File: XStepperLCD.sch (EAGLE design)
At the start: 7 parts, among them U1 Attiny85

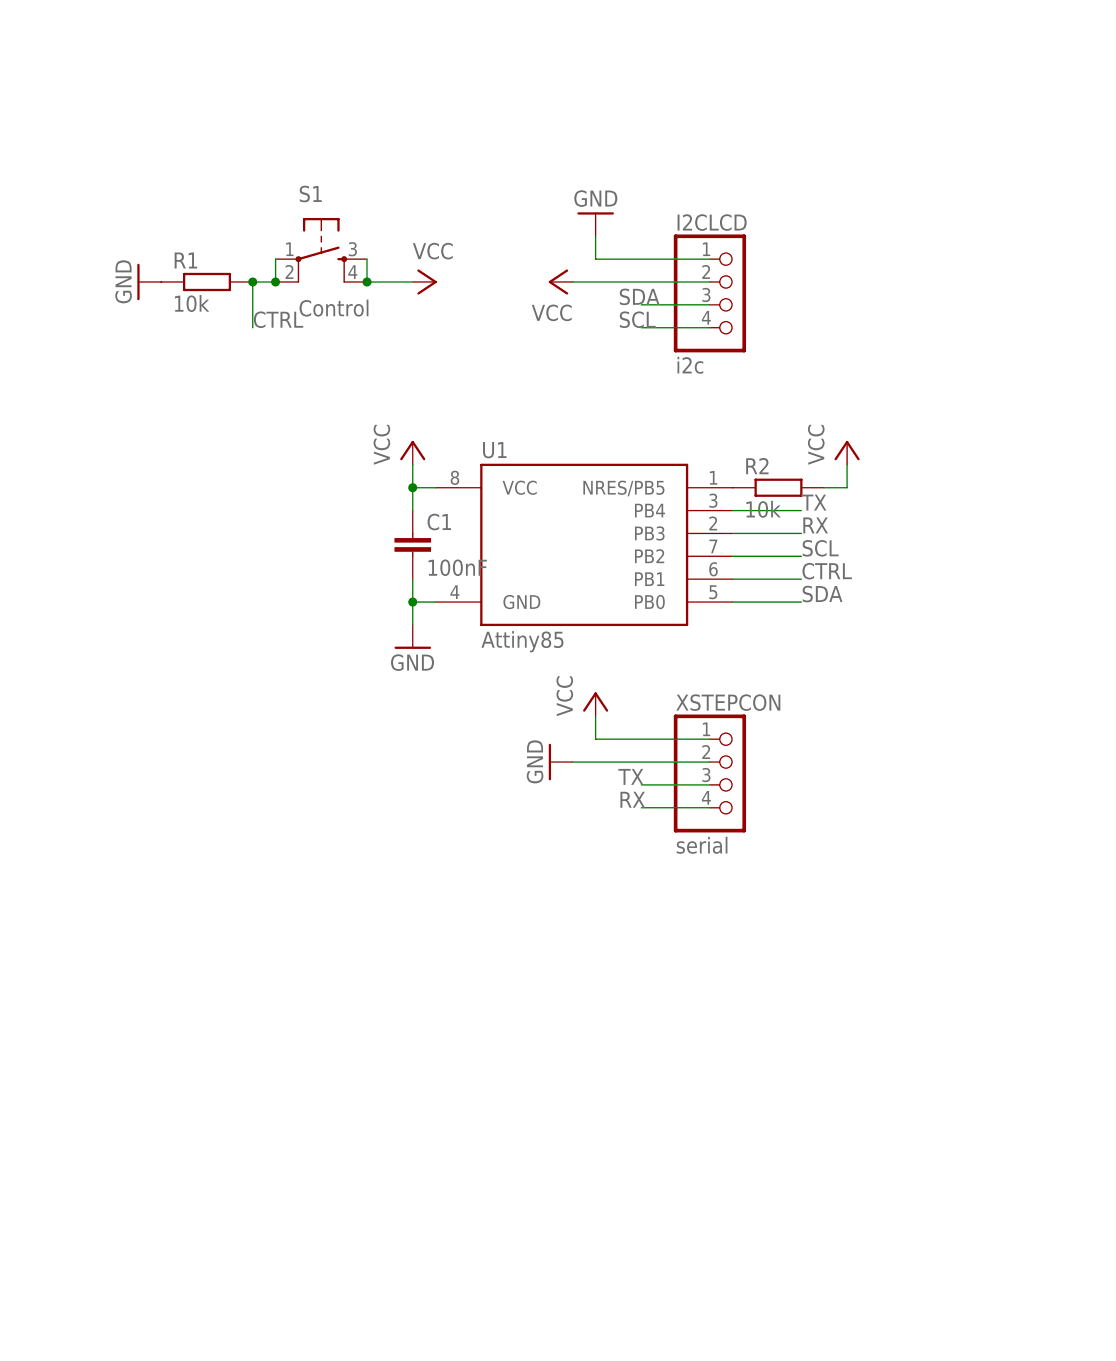
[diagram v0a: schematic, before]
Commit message: First konzept for XLCD with 328p
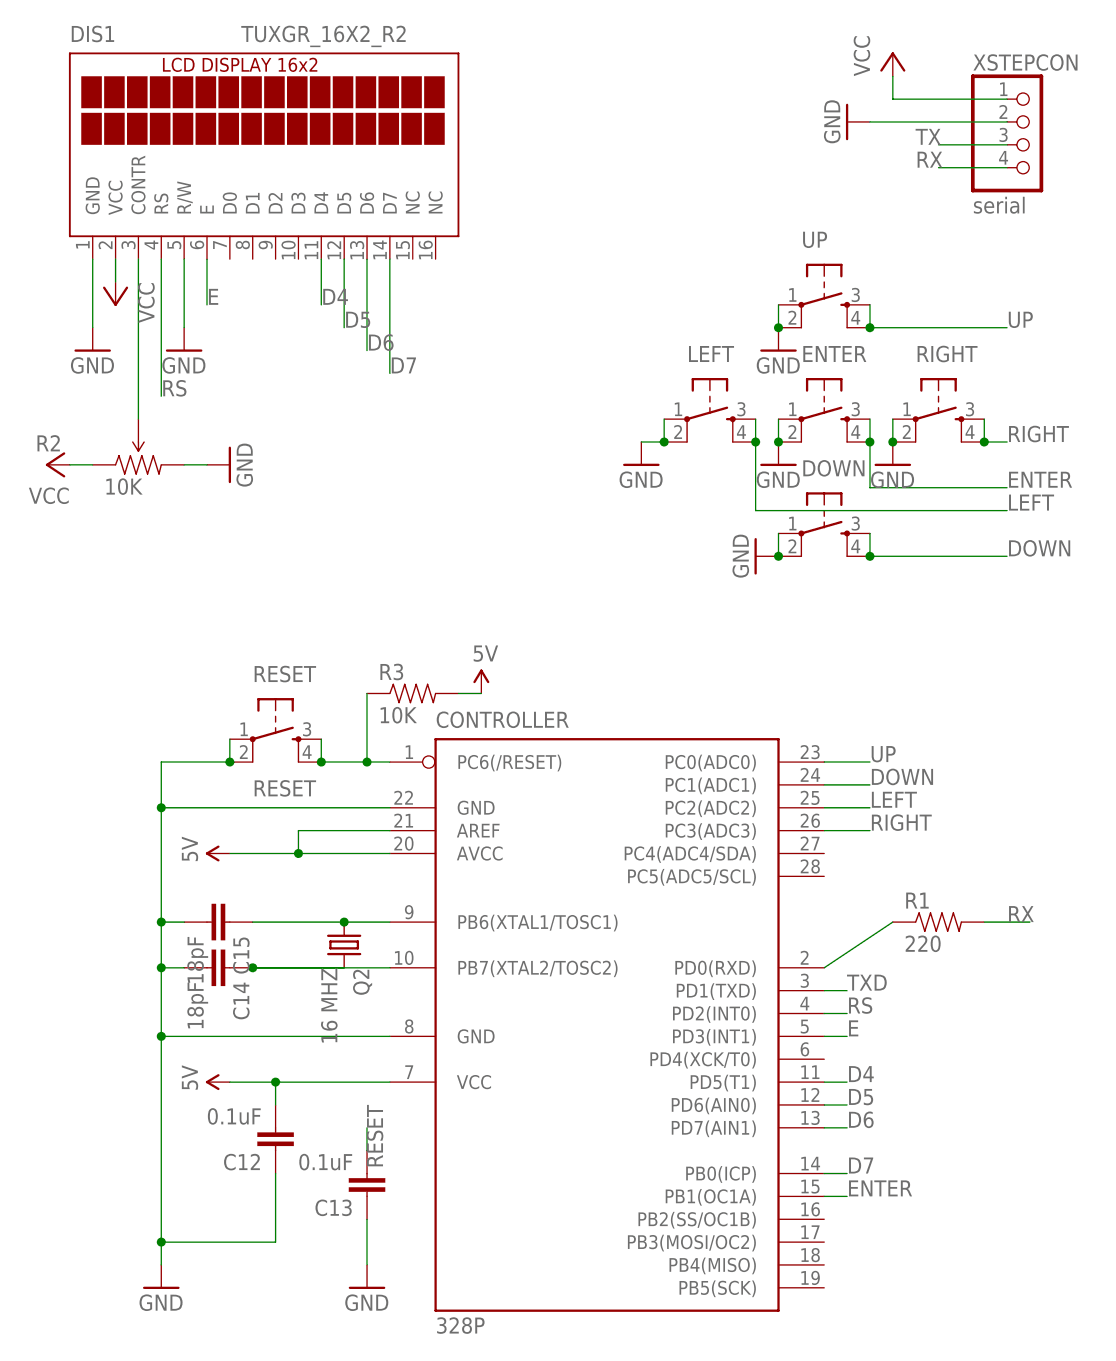
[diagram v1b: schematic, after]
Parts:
- removed C1: 100nF, rcl:C-EU025-025X050
- removed I2CLCD: i2c, pinhead:PINHD-1X4/90
- removed S1: Control, SparkFun-Electromechanical:TAC_SWITCHPTH
- removed U1: Attiny85, _hhn_attiny25_45_85:ATTINY85V-10P
- added 328P: CONTROLLER, Bibsatmel:MEGA8-P
- added C12, C13: 0.1uF, resistor:C-EU025-025X050
- added C14, C15: 18pF, resistor:C-EU025-025X050
- added DIS1: TUXGR_16X2_R2, display-lcd:TUXGR_16X2_R2
- added DOWN, ENTER, LEFT, RIGHT, UP: (no value), SparkFun:TAC_SWITCHPTH
- added Q2: 16 MHZ, crystal:CRYSTALHC49S
- added R3: 10K, SparkFun-Resistors:RESISTORAXIAL-0.3
- added RESET: RESET, SparkFun:TAC_SWITCHPTH
- R1: value 10k -> 220; device resistor:R-EU_0204/7 -> SparkFun-Resistors:RESISTORAXIAL-0.3
- R2: value 10k -> 10K; device resistor:R-EU_0204/7 -> SparkFun-Electromechanical:TRIMPOT-PTH-KNOB
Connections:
- removed net CTRL: R1.2, S1.1, S1.2, U1.PB1
- removed net SCL: I2CLCD.4, U1.PB2
- removed net SDA: I2CLCD.3, U1.PB0
- new net 5V: 328P.AREF, 328P.AVCC, 328P.VCC@1, C12.2, R3.2
- new net D4: 328P.PD5(T1), DIS1.D4
- new net D5: 328P.PD6(AIN0), DIS1.D5
- new net D6: 328P.PD7(AIN1), DIS1.D6
- new net D7: 328P.PB0(ICP), DIS1.D7
- new net DOWN: 328P.PC1(ADC1), DOWN.3, DOWN.4
- new net E: 328P.PD3(INT1), DIS1.E
- new net ENTER: 328P.PB1(OC1A), ENTER.3, ENTER.4
- new net LEFT: 328P.PC2(ADC2), LEFT.3, LEFT.4
- new net N$2: DIS1.CONTR, R2.WIPER
- new net N$33: 328P.PB6(XTAL1/TOSC1), C15.1, Q2.1
- new net N$34: 328P.PB7(XTAL2/TOSC2), C14.1, Q2.2
- new net RESET: 328P.PC6(/RESET), C13.2, R3.1, RESET.3, RESET.4
- new net RIGHT: 328P.PC3(ADC3), RIGHT.3, RIGHT.4
- new net RS: 328P.PD2(INT0), DIS1.RS
- new net TXD: 328P.PD1(TXD)
- new net UP: 328P.PC0(ADC0), UP.3, UP.4
- net GND: now also 328P.GND, 328P.GND@1, C12.1, C13.1, C14.2, C15.2, DIS1.GND, DIS1.R/W, DOWN.1, DOWN.2, ENTER.1, ENTER.2, LEFT.1, LEFT.2, R2.CW, RESET.1, RESET.2, RIGHT.1, RIGHT.2, UP.1, UP.2; no longer C1.2, I2CLCD.1, R1.1, U1.GND
- net N$1: now also 328P.PD0(RXD), R1.1; no longer R2.1, U1.NRES/PB5
- net RX: now also R1.2; no longer U1.PB3
- net TX: no longer U1.PB4
- net VCC: now also DIS1.VCC, R2.CCW; no longer C1.1, I2CLCD.2, R2.2, S1.3, S1.4, U1.VCC
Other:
- moved on the sheet: XSTEPCON

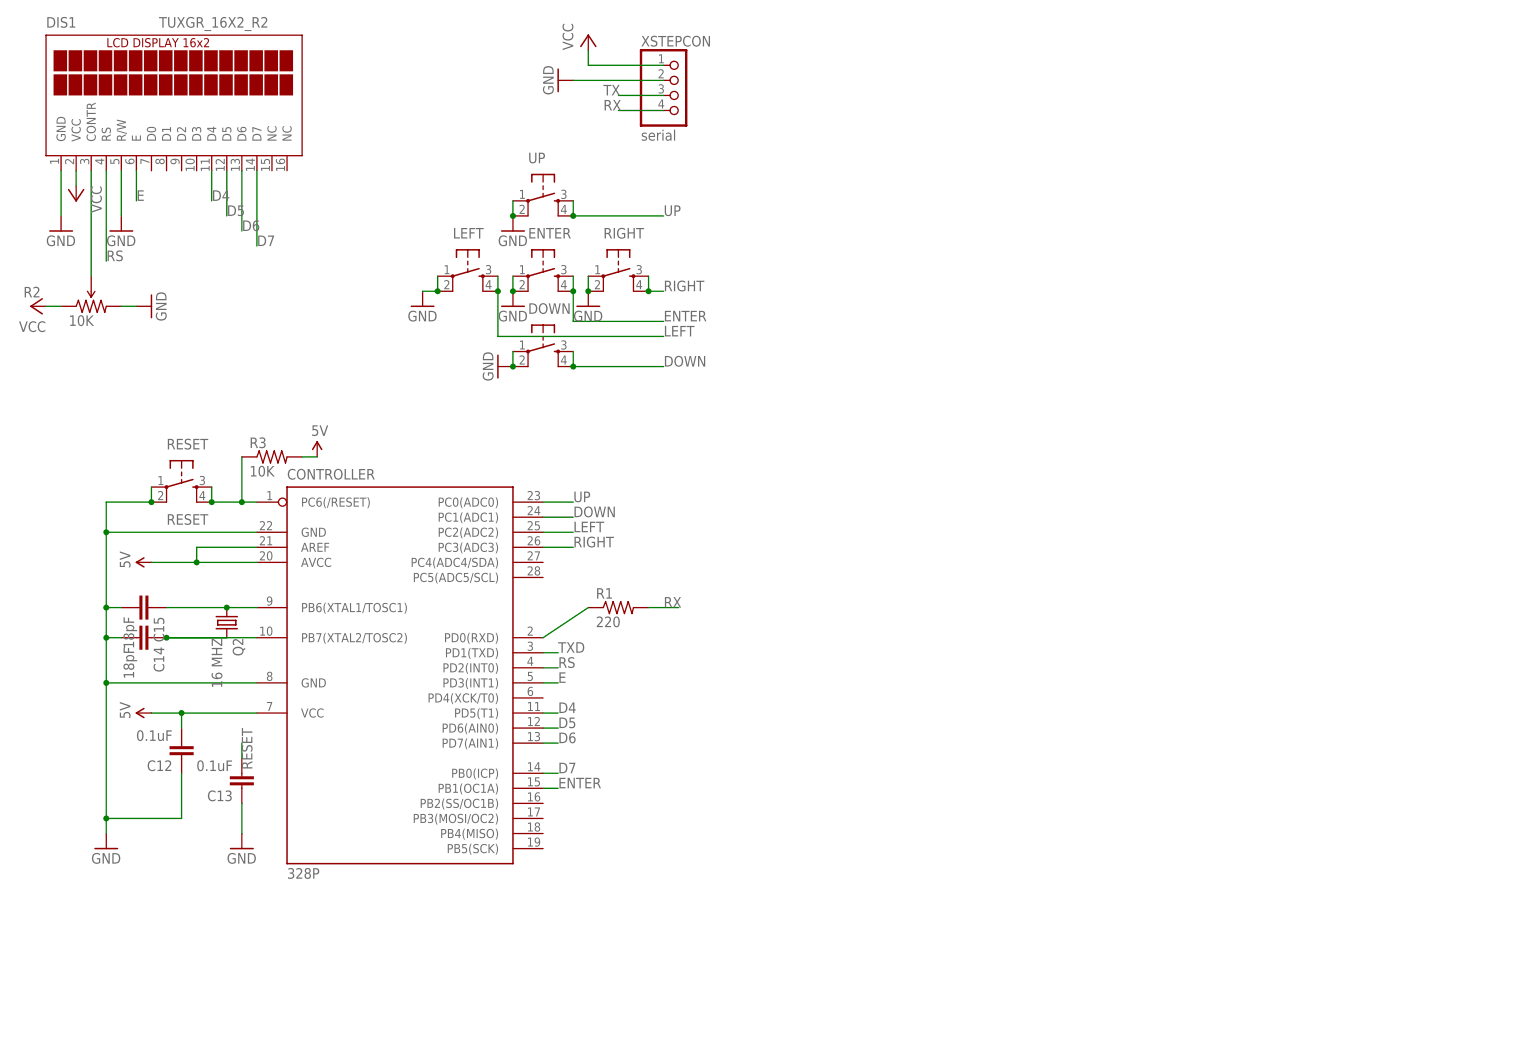
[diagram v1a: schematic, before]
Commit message: add conn header for buttons
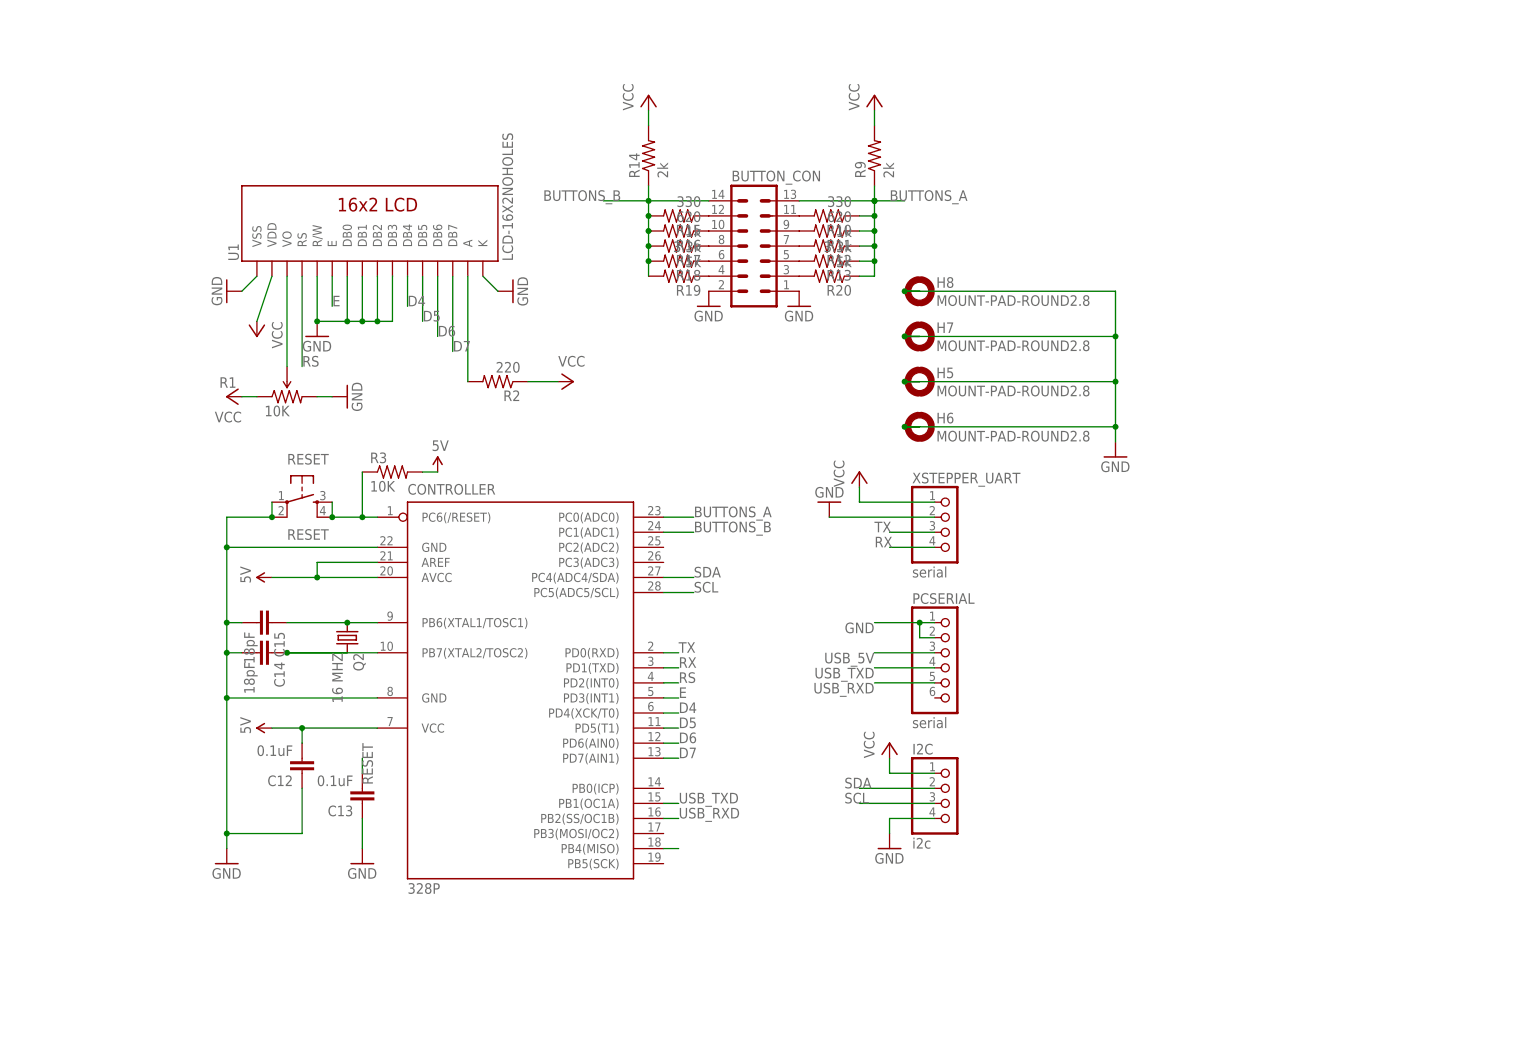
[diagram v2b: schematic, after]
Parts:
- removed DIS1: TUXGR_16X2_R2, display-lcd:TUXGR_16X2_R2
- removed DOWN, ENTER, LEFT, RIGHT, UP: (no value), SparkFun:TAC_SWITCHPTH
- removed XSTEPCON: serial, pinhead:PINHD-1X4/90
- added BUTTON_CON: (no value), con-ml:ML14
- added H5, H6, H7, H8: MOUNT-PAD-ROUND2.8, holes:MOUNT-PAD-ROUND2.8
- added I2C: i2c, pinhead:PINHD-1X4/90
- added PCSERIAL: serial, pinhead:PINHD-1X6/90
- added R10, R15: 330, SparkFun-Resistors:RESISTORAXIAL-0.3
- added R11, R16: 620, SparkFun-Resistors:RESISTORAXIAL-0.3
- added R12, R17: 1k, SparkFun-Resistors:RESISTORAXIAL-0.3
- added R13, R18: 3.3k, SparkFun-Resistors:RESISTORAXIAL-0.3
- added R14, R9: 2k, SparkFun-Resistors:RESISTORAXIAL-0.3
- added R19, R20: 5k, SparkFun-Resistors:RESISTORAXIAL-0.3
- added U1: LCD-16X2NOHOLES, SparkFun-Displays:LCD-16X2NOHOLES
- added XSTEPPER_UART: serial, pinhead:PINHD-1X4/90
- R1: value 220 -> 10K; device SparkFun-Resistors:RESISTORAXIAL-0.3 -> SparkFun-Electromechanical:TRIMPOT-PTH-KNOB
- R2: value 10K -> 220; device SparkFun-Electromechanical:TRIMPOT-PTH-KNOB -> SparkFun-Resistors:RESISTORAXIAL-0.3
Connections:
- removed net DOWN: 328P.PC1(ADC1), DOWN.3, DOWN.4
- removed net ENTER: 328P.PB1(OC1A), ENTER.3, ENTER.4
- removed net LEFT: 328P.PC2(ADC2), LEFT.3, LEFT.4
- removed net RIGHT: 328P.PC3(ADC3), RIGHT.3, RIGHT.4
- removed net TXD: 328P.PD1(TXD)
- removed net UP: 328P.PC0(ADC0), UP.3, UP.4
- new net BUTTONS_A: 328P.PC0(ADC0), BUTTON_CON.13, R10.1, R11.1, R12.1, R13.1, R20.1, R9.1
- new net BUTTONS_B: 328P.PC1(ADC1), BUTTON_CON.14, R14.1, R15.2, R16.2, R17.2, R18.2, R19.2
- new net N$11: BUTTON_CON.12, R15.1
- new net N$12: BUTTON_CON.10, R16.1
- new net N$13: BUTTON_CON.8, R17.1
- new net N$14: BUTTON_CON.6, R18.1
- new net N$15: BUTTON_CON.4, R19.1
- new net N$16: BUTTON_CON.3, R20.2
- new net N$3: BUTTON_CON.11, R10.2
- new net N$4: BUTTON_CON.9, R11.2
- new net N$5: BUTTON_CON.7, R12.2
- new net N$6: BUTTON_CON.5, R13.2
- new net SCL: 328P.PC5(ADC5/SCL), I2C.3
- new net SDA: 328P.PC4(ADC4/SDA), I2C.2
- new net USB_5V: PCSERIAL.3
- new net USB_RXD: 328P.PB2(SS/OC1B), PCSERIAL.5
- new net USB_TXD: 328P.PB1(OC1A), PCSERIAL.4
- net D4: now also U1.DB4; no longer 328P.PD5(T1), DIS1.D4
- net D5: now also 328P.PD5(T1), U1.DB5; no longer 328P.PD6(AIN0), DIS1.D5
- net D6: now also 328P.PD6(AIN0), U1.DB6; no longer 328P.PD7(AIN1), DIS1.D6
- net D7: now also 328P.PD7(AIN1), U1.DB7; no longer 328P.PB0(ICP), DIS1.D7
- net E: now also U1.E; no longer DIS1.E
- net GND: now also BUTTON_CON.1, BUTTON_CON.2, H5.MOUNT, H6.MOUNT, H7.MOUNT, H8.MOUNT, I2C.4, PCSERIAL.1, PCSERIAL.2, R1.CW, U1.DB0, U1.DB1, U1.DB2, U1.DB3, U1.K, U1.R/W, U1.VSS, XSTEPPER_UART.2; no longer DIS1.GND, DIS1.R/W, DOWN.1, DOWN.2, ENTER.1, ENTER.2, LEFT.1, LEFT.2, R2.CW, RIGHT.1, RIGHT.2, UP.1, UP.2, XSTEPCON.2
- net N$1: now also R1.WIPER, U1.VO; no longer 328P.PD0(RXD), R1.1
- net N$2: now also R2.2, U1.A; no longer DIS1.CONTR, R2.WIPER
- net RS: now also U1.RS; no longer DIS1.RS
- net RX: now also 328P.PD1(TXD), XSTEPPER_UART.4; no longer R1.2, XSTEPCON.4
- net TX: now also 328P.PD0(RXD), XSTEPPER_UART.3; no longer XSTEPCON.3
- net VCC: now also I2C.1, R1.CCW, R14.2, R2.1, R9.2, U1.VDD, XSTEPPER_UART.1; no longer DIS1.VCC, R2.CCW, XSTEPCON.1
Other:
- moved on the sheet: 328P, C12, C13, C14, C15, Q2, R3, RESET
